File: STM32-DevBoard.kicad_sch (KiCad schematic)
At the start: 55 parts, among them J1 I2C Bus 1, J2 Serial Debugger, J3 USART1, J4 12402012E212A, J5 PJ-002A, Q1 AO3401A, SW1 SW_SPDT, U1 STM32F103C8T6, U2 TPS563209DDCR, U3 USBLC6-2SC6, Y1 16MHz

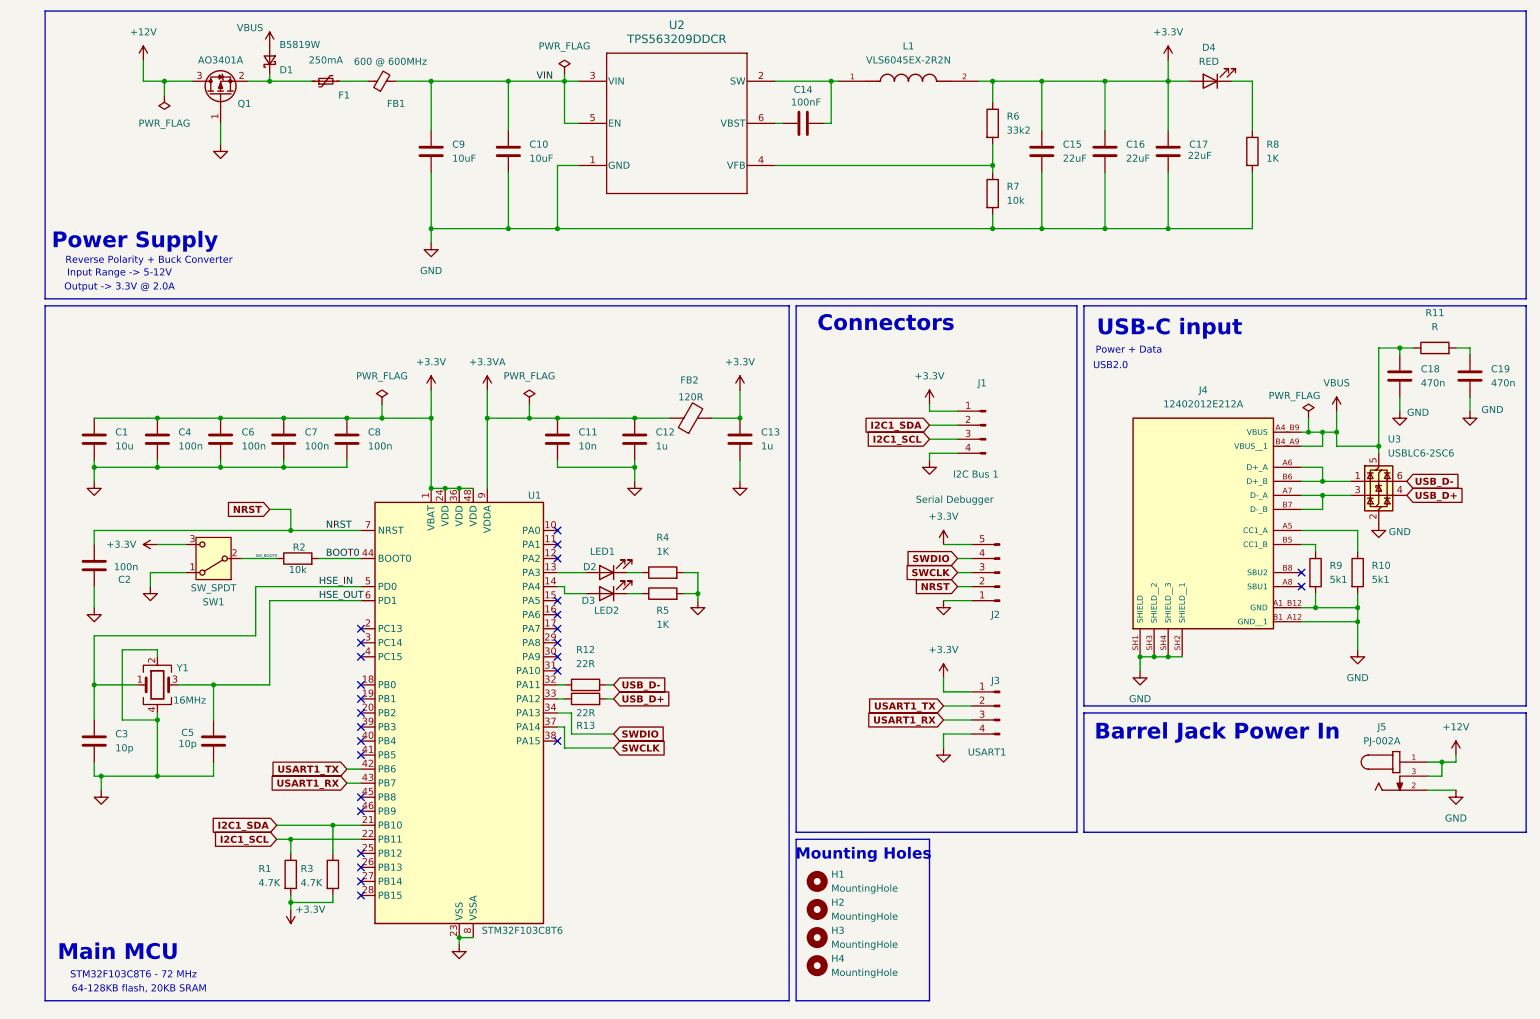
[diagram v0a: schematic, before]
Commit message: Board constraints, layout, and initial traces done
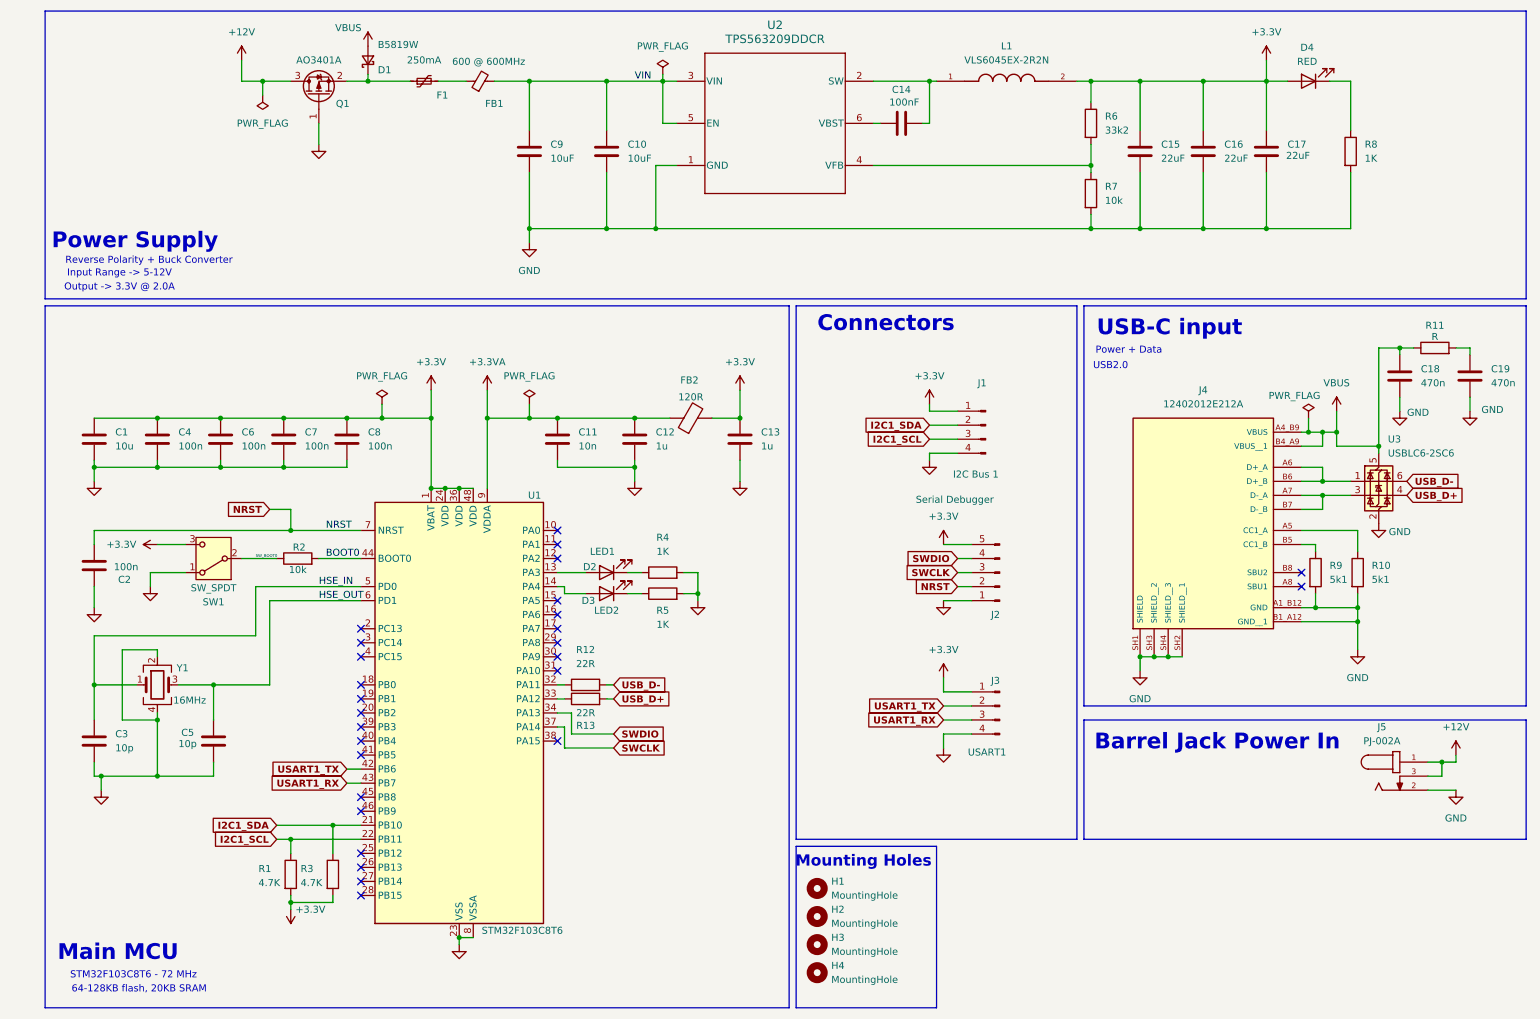
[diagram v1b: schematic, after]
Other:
- moved on the sheet: C10, C14, C15, C16, C17, C9, D1, D4, F1, FB1, H1, H2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

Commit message: extra gpio
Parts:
- added J6: Conn_01x08_Pin, symbol Connector:Conn_01x08_Pin
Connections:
- net +3.3V: now also J6.2 (Pin_2)
- net GND: now also J6.1 (Pin_1)
- net at D3.2 (A): now also U1.12 (PA2); no longer U1.14 (PA4)
- net GPIO6: now reaches U1.10 (PA0)
- net GPIO6: now also J6.8 (Pin_8)
- net at U1.11 (PA1): now also D2.2 (A)
- net GPIO1: now reaches U1.13 (PA3)
- net GPIO1: now also J6.3 (Pin_3); no longer D2.2 (A)
- net GPIO3: now reaches U1.15 (PA5)
- net GPIO3: now also J6.5 (Pin_5)
- net GPIO4: now reaches U1.16 (PA6)
- net GPIO4: now also J6.6 (Pin_6)
- net GPIO5: now reaches U1.17 (PA7)
- net GPIO5: now also J6.7 (Pin_7)
- new net GPIO2: J6.4 (Pin_4), U1.14 (PA4)
- no-connect marks 27 -> 22
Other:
- moved on the sheet: D2, D3, R4, R5

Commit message: part descs
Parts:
- Q1: Manufacturer (none) -> AOS; Manufacturer Part # (none) -> AO3401A
- U1: Distributor Link 1 (none) -> https://www.digikey.com.au/en/products/detail/stmicroelectr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; Distributor Link 2 (none) -> https://au.mouser.com/ProductDetail/STMicroelectronics/STM3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; Manufacturer Part # (none) -> STM32F103C8T6
- U2: Distributor Link 1 (none) -> https://www.digikey.com.au/en/products/detail/texas-instrum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; Distributor Link 2 (none) -> https://au.mouser.com/ProductDetail/Texas-Instruments/TPS56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; LCSC (none) -> C181974; Manufacturer (none) -> Texas Instruments; Manufacturer Part # (none) -> TPS563209DDCR
- U3: Distributor 1 (none) -> https://au.mouser.com/ProductDetail/STMicroelectronics/USBL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; Distributor 2 (none) -> https://www.digikey.com.au/en/products/detail/stmicroelectr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; LCSC (none) -> C7519; Manufacturer (none) -> STMicroelectronics; Manufacturer Part # (none) -> USBLC6-2SC6
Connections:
- net VBUS: no longer D1.2 (A)
- net VBUSF: now reaches C19.1, R11.2
- net VBUSF: now also D1.2 (A)
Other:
- moved on the sheet: D1, D3, R5

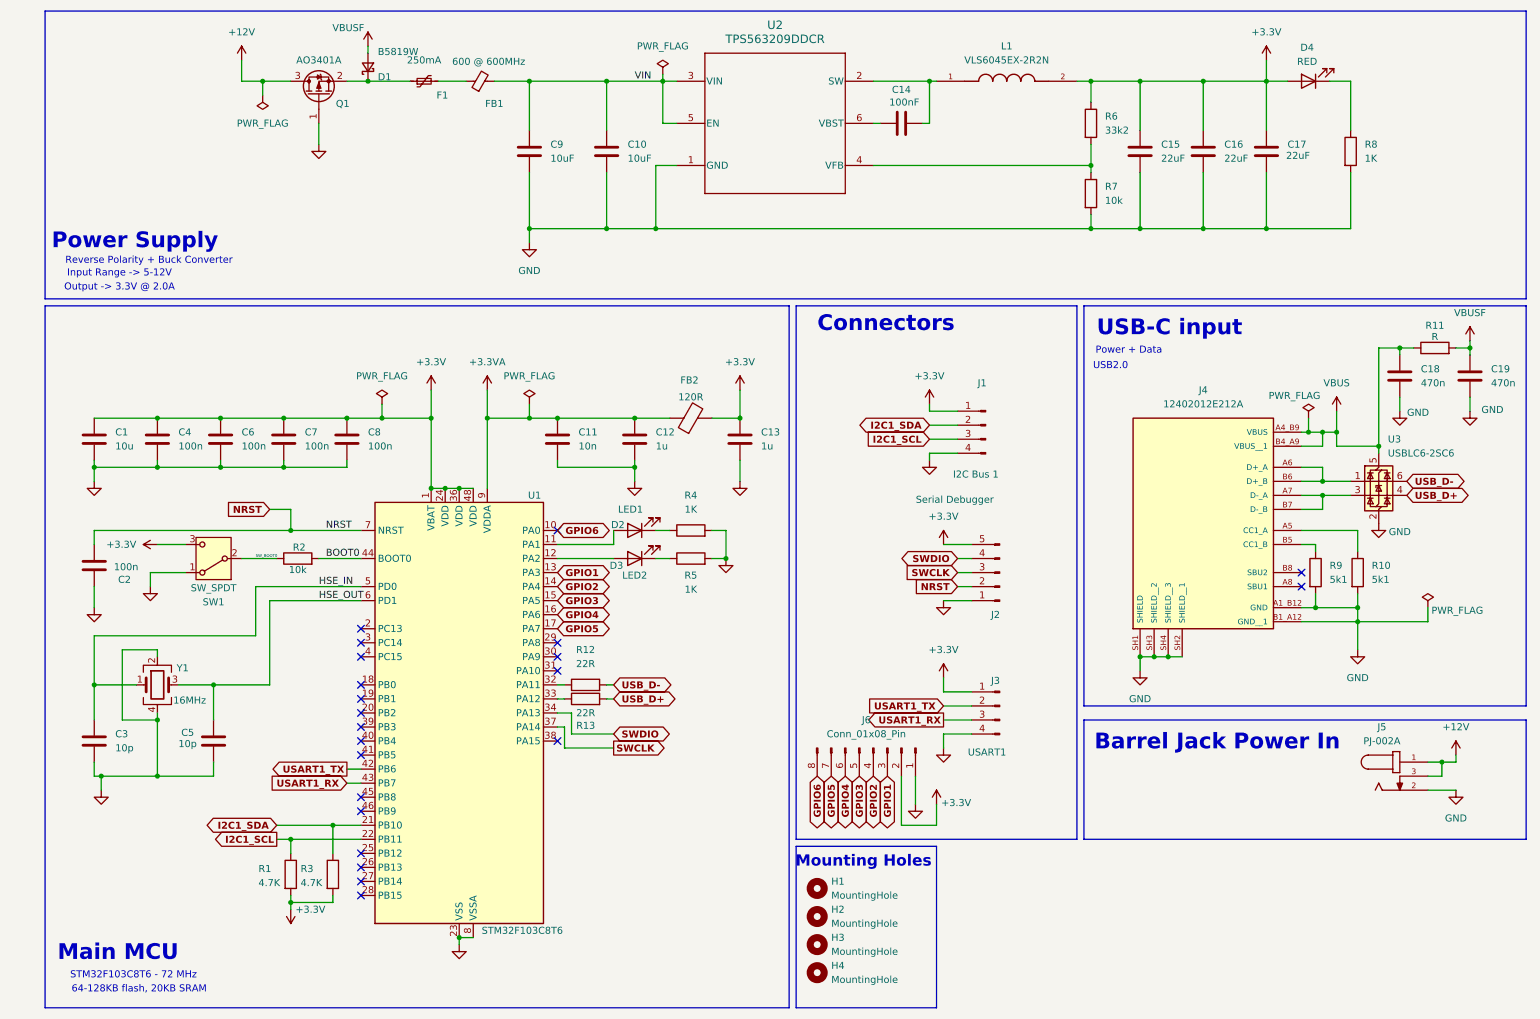
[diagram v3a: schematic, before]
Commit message: Added component information
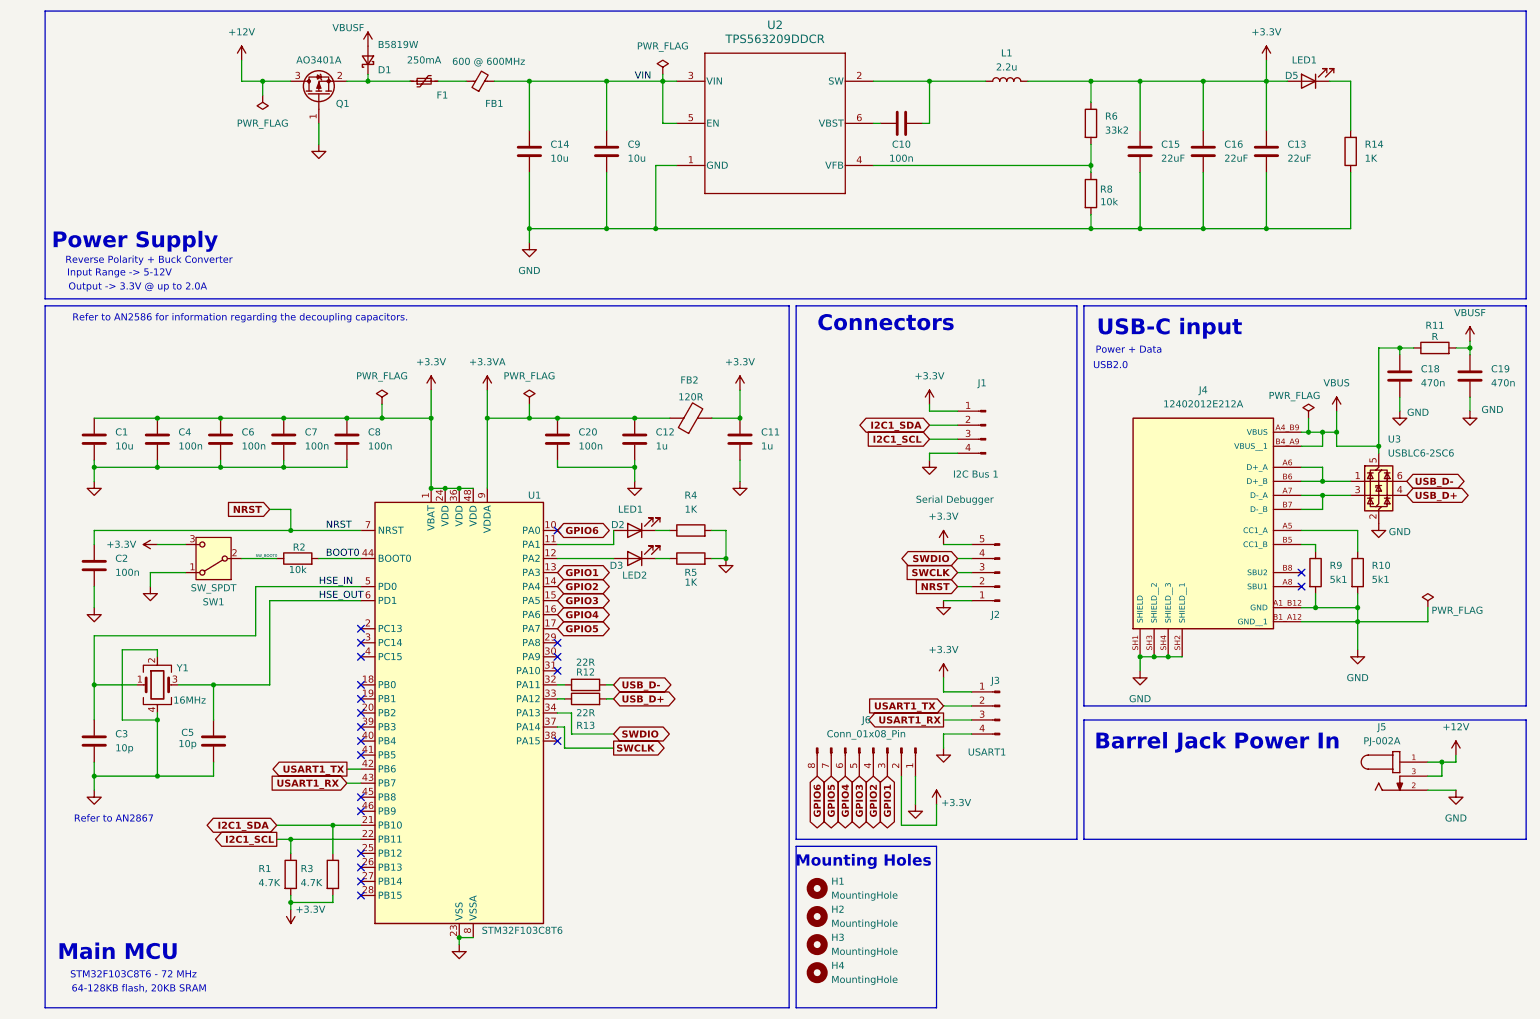
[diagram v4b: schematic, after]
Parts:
- removed C17: 22uF, Capacitor_SMD:C_0603_1608Metric, symbol Device:C
- removed D4: RED, LED_SMD:LED_0603_1608Metric, symbol Device:LED
- removed L1: VLS6045EX-2R2N, Footprints:IND_VLS6045EX-2R2N, symbol VLS6045EX-2R2N:VLS6045EX-2R2N
- removed R7: 10k, Resistor_SMD:R_0402_1005Metric, symbol Device:R
- added C20: 100n, Capacitor_SMD:C_0402_1005Metric, symbol Device:C
- added D5: LED1, LED_SMD:LED_0603_1608Metric, symbol Device:LED
- added L1: 2.2u, symbol Device:L
- added R14: 1K, Resistor_SMD:R_0402_1005Metric, symbol Device:R
- C1: footprint Capacitor_SMD:C_0603_1608Metric -> Capacitor_SMD:C_0805_2012Metric; LCSC Part # C91606 -> C15850
- C10: value 10uF -> 100n; footprint Capacitor_SMD:C_0805_2012Metric -> Capacitor_SMD:C_0402_1005Metric; LCSC (none) -> C1525; Manufacturer Part # (none) -> CL05B104KO5NNNC
- C11: value 10n -> 1u; LCSC (none) -> C52923; LCSC Part # C1524 -> (none)
- C12: LCSC (none) -> C52923; LCSC Part # C29266 -> (none)
- C13: value 1u -> 22uF; footprint Capacitor_SMD:C_0402_1005Metric -> Capacitor_SMD:C_0603_1608Metric; LCSC (none) -> C59461; LCSC Part # C29266 -> (none)
- C14: value 100nF -> 10u; LCSC Part # (none) -> C15850
- C16: LCSC (none) -> C59461
- C2, C4, C6, C7, C8: LCSC (none) -> C1525; LCSC Part # C1525 -> (none); Manufacturer Part # (none) -> CL05B104KO5NNNC
- C3, C5: LCSC (none) -> C32949; LCSC Part # C1545 -> (none)
- C9: value 10uF -> 10u; LCSC Part # (none) -> C15850
- D1: LCSC Part # C64885 -> C8598
- D2, D3: LCSC (none) -> C2290
- FB2: LCSC Part # C14710 -> C14709
- R1, R3: LCSC (none) -> C25900
- R10, R4, R5, R9: LCSC (none) -> C11702
- R12, R13: LCSC (none) -> C1091
- R8: value 1K -> 10k; LCSC Part # (none) -> C25744
- SW1: LCSC Part # C221841 -> C109335
- Y1: LCSC (none) -> C112972; LCSC Part # C13738 -> (none)
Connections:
- net +3.3V: now also C11.1, D5.2 (A), L1.2
- net +3.3VA: now also C20.1; no longer C11.1
- net GND: now also C14.2, C20.2, R14.1; no longer C10.2
- net VIN: now also C14.1; no longer C10.1
- net at U2.2 (SW): now also C10.1, L1.1; no longer C14.2
- net at R6.2, U2.4 (VFB): now also R8.1
- net at U2.6 (VBST): now also C10.2; no longer C14.1
- new net: D5.1 (K), R14.2
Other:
- note added: "Output -> 3.3V @ up to 2.0A"
- note added: "Refer to AN2586 for information regarding the decoupling capacitors."
- note added: "Refer to AN2867"
- note removed: "Output -> 3.3V @ 2.0A"
- moved on the sheet: D1

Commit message: Added a bit more component information
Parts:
- J5: renamed from J4; LCSC (none) -> C5150972
- J6: renamed from J5; LCSC (none) -> C3096082
- renumbered C20 to C10, C9 to C11, C11 to C13, C10 to C14, C13 to C17, C14 to C9, D5 to D4, J6 to J1, J1 to J2, J2 to J3, J3 to J4, R9 to R10, R14 to R11, R10 to R12, R11 to R13, R12 to R4, R13 to R5, R4 to R6, R5 to R7, R6 to R8, R8 to R9

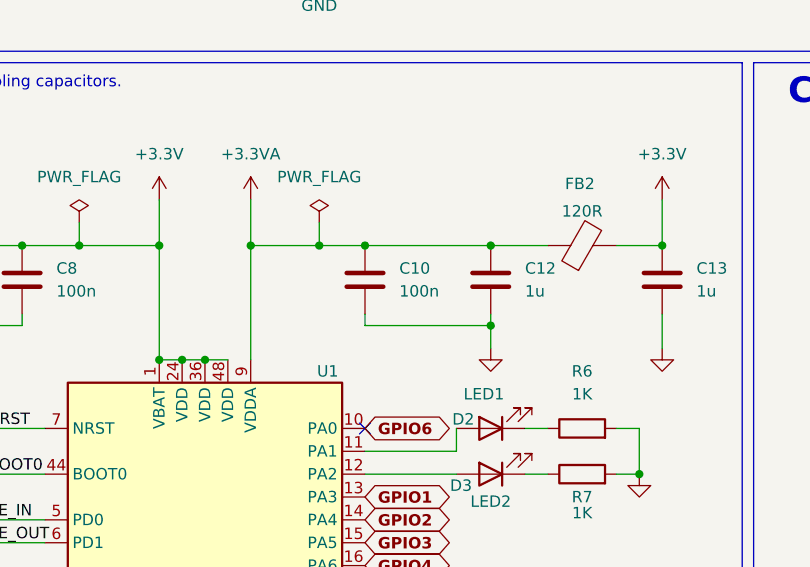
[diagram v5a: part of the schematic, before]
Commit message: Added footprints and models, progressed PCB layout. TODO: rename nets
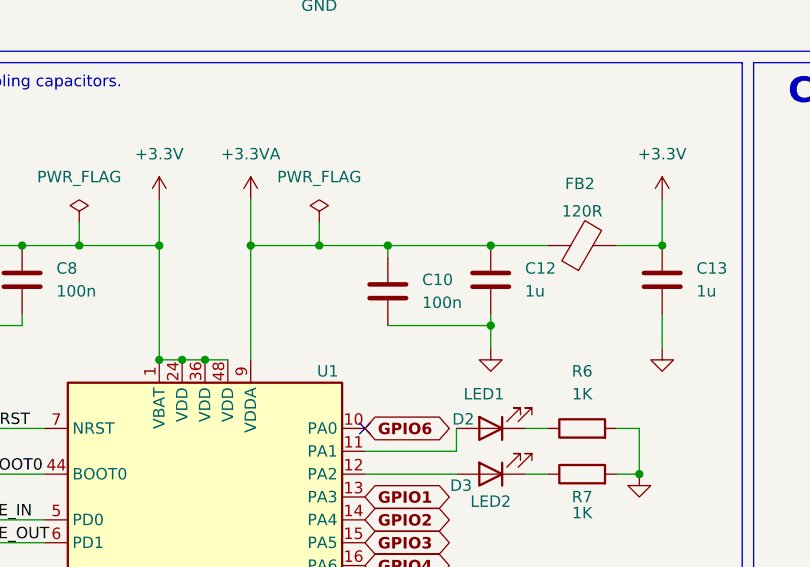
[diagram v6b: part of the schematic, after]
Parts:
- J1: footprint (none) -> Connector_PinHeader_1.00mm:PinHeader_1x08_P1.00mm_Vertical
- L1: footprint (none) -> Footprints:IND_VLS6045EX-2R2N
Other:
- moved on the sheet: C10
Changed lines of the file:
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@@
 	)
 	(junction
+		(at 110.49 88.9)
+		(diameter 0)
+		(color 0 0 0 0)
+	)
+	(junction
 		(at 246.38 102.87)
 		(diameter 0)
@@
 	)
 	(junction
-		(at 107.95 88.9)
-		(diameter 0)
-		(color 0 0 0 0)
-	)
-	(junction
 		(at 87.63 101.6)
 		(diameter 0)
@@
 	(wire
 		(pts
-			(xy 107.95 88.9) (xy 121.92 88.9)
-		)
-		(stroke
-			(width 0)
-			(type default)
-		)
-	)
-	(wire
-		(pts
 			(xy 245.11 120.65) (xy 245.11 123.19)
 		)
@@
 	(wire
 		(pts
-			(xy 121.92 97.79) (xy 107.95 97.79)
+			(xy 121.92 97.79) (xy 110.49 97.79)
 		)
 		(stroke
@@
 	(wire
 		(pts
-			(xy 107.95 97.79) (xy 107.95 96.52)
-		)
-		(stroke
-			(width 0)
-			(type default)
-		)
-	)
-	(wire
-		(pts
 			(xy 67.31 162.56) (xy 67.31 167.64)
 		)
@@
 	(wire
 		(pts
+			(xy 110.49 88.9) (xy 121.92 88.9)
+		)
+		(stroke
+			(width 0)
+			(type default)
+		)
+	)
+	(wire
+		(pts
 			(xy 243.84 91.44) (xy 246.38 91.44)
 		)
@@
 	(wire
 		(pts
-			(xy 102.87 88.9) (xy 107.95 88.9)
+			(xy 102.87 88.9) (xy 110.49 88.9)
 		)
 		(stroke
@@
 	(wire
 		(pts
+			(xy 110.49 90.17) (xy 110.49 88.9)
+		)
+		(stroke
+			(width 0)
+			(type default)
+		)
+	)
+	(wire
+		(pts
 			(xy 24.13 97.79) (xy 35.56 97.79)
 		)
@@
 	(symbol
 		(lib_id "Device:C")
-		(at 107.95 92.71 0)
+		(at 110.49 93.98 0)
 		(unit 1)
 		(exclude_from_sim no)
@@
 		(fields_autoplaced yes)
 		(property "Reference" "C10"
-			(at 111.76 91.4399 0)
+			(at 114.3 92.7099 0)
 			(effects
 				(font
@@
 		)
 		(property "Value" "100n"
-			(at 111.76 93.9799 0)
+			(at 114.3 95.2499 0)
 			(effects
 				(font
@@
 		)
 		(property "Footprint" "Capacitor_SMD:C_0402_1005Metric"
-			(at 108.9152 96.52 0)
+			(at 111.4552 97.79 0)
 			(effects
 				(font
@@
 		)
 		(property "Datasheet" "~"
-			(at 107.95 92.71 0)
+			(at 110.49 93.98 0)
 			(effects
 				(font
@@
 		)
 		(property "Description" "Unpolarized capacitor"
-			(at 107.95 92.71 0)
+			(at 110.49 93.98 0)
 			(effects
 				(font
@@
 		)
 		(property "LCSC" "C1525"
-			(at 107.95 92.71 0)
+			(at 110.49 93.98 0)
 			(effects
 				(font
@@
 		)
 		(property "Manufacturer Part #" "CL05B104KO5NNNC"
-			(at 107.95 92.71 0)
+			(at 110.49 93.98 0)
 			(effects
 				(font
@@
 			)
 		)
-		(property "Footprint" ""
+		(property "Footprint" "Connector_PinHeader_1.00mm:PinHeader_1x08_P1.00mm_Vertical"
 			(at 165.1 148.59 0)
 			(effects
@@
 			)
 		)
-		(property "Footprint" ""
+		(property "Footprint" "Footprints:IND_VLS6045EX-2R2N"
 			(at 189.23 27.94 0)
 			(effects
